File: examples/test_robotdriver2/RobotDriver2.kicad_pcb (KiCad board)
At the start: 2 copper layers, 125 x 75 mm, 68 parts, among them J1 C64658, J3 C265088, J4 C265088, J6 C64658, J7 C64658, J8 C64658, J9 C64658, SW1 C318884, U1 C7972, U2 C500769, U3 C701342, U4 C967633, U5 C50506, U6 C50506

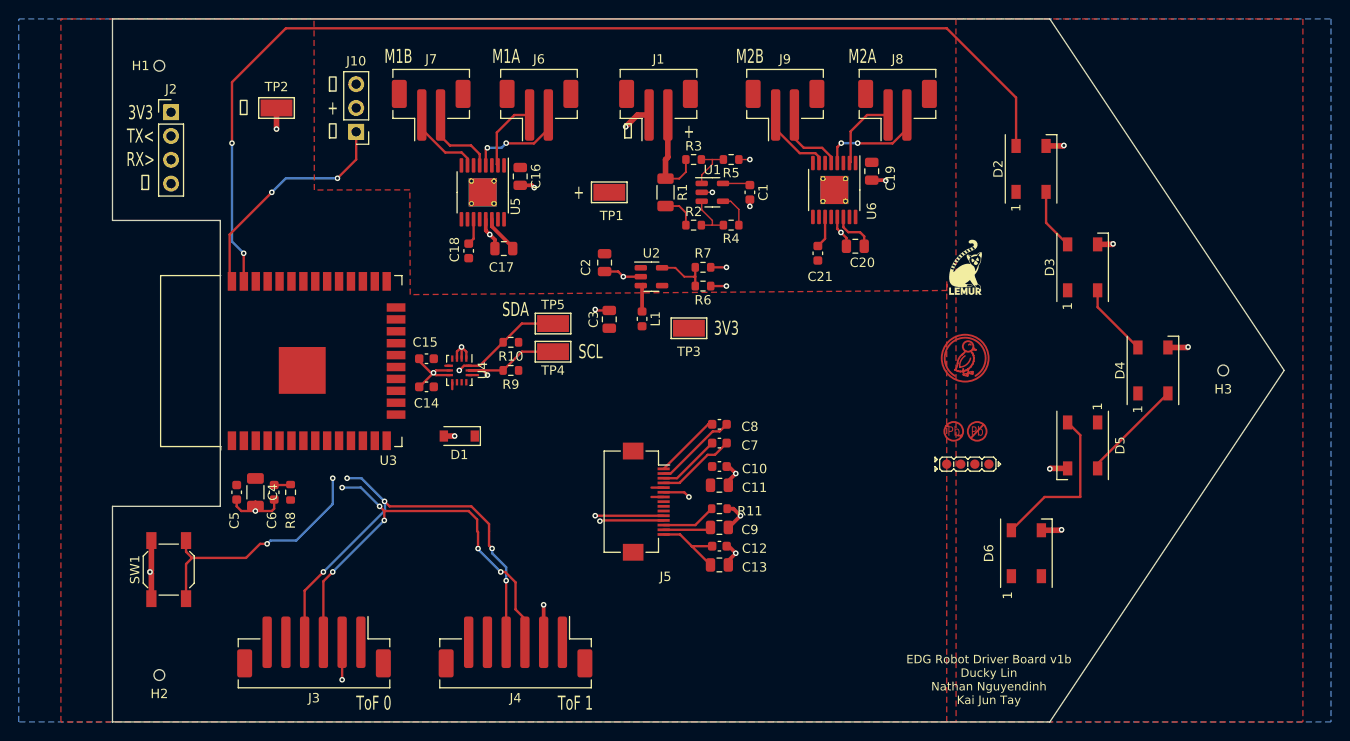
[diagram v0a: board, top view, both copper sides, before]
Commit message: robot driver 2 layout wip floorplanned
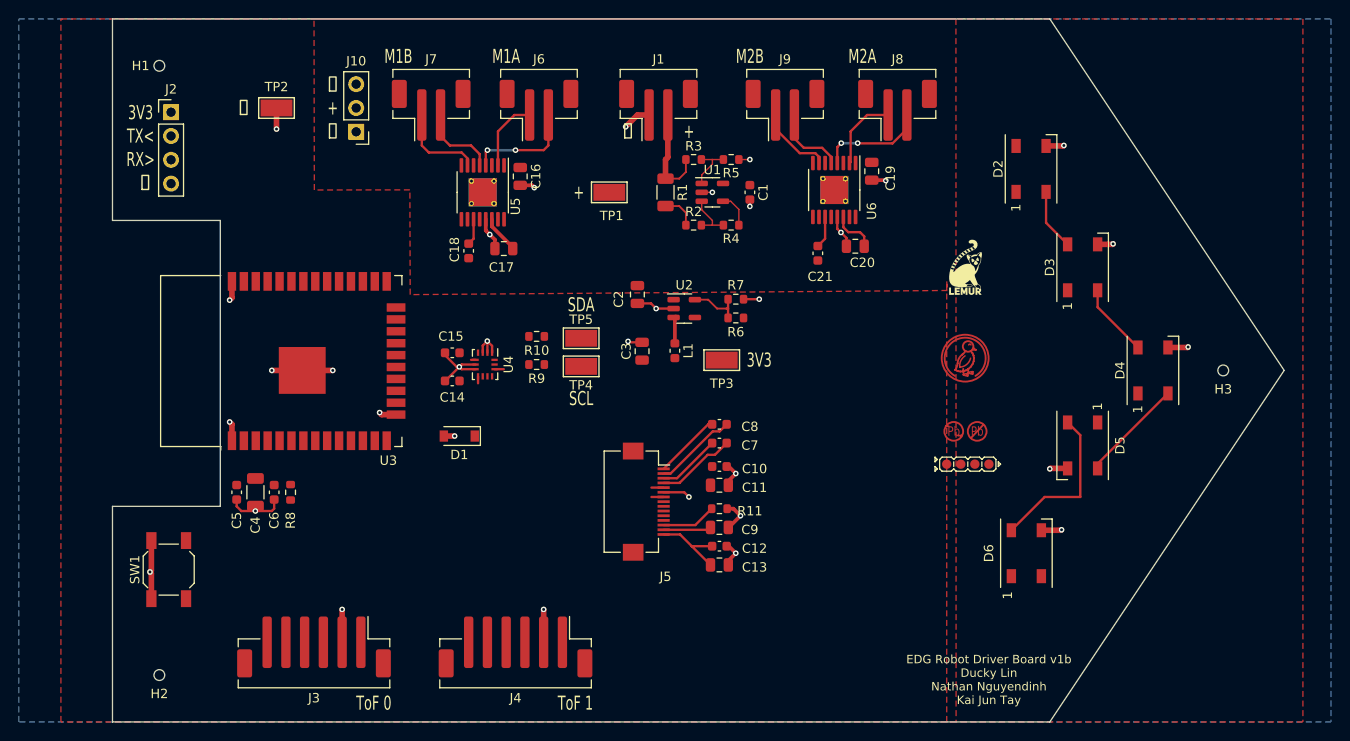
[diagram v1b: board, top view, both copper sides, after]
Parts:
- moved C2 4.88 mm to (151.0, 76.9)
- moved C3 4.88 mm to (151.5, 83.0)
- moved L1 4.88 mm to (155.0, 82.9)
- moved R6 4.88 mm to (161.5, 79.4)
- moved R7 4.88 mm to (161.5, 77.4)
- moved TP3 4.88 mm to (160.0, 83.9)
- moved U2 4.88 mm to (156.0, 78.4)
- moved TP4 3.39 mm to (145.0, 84.6)
- moved TP5 3.39 mm to (145.0, 81.6)
- moved C14 2.82 mm to (131.2, 86.1)
- moved C15 2.82 mm to (131.2, 83.1)
- moved R10 2.82 mm to (140.2, 81.4)
- moved R9 2.82 mm to (140.2, 84.4)
- moved U4 2.82 mm to (134.8, 84.4)
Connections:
- net isense.amp.(adapter)r1.b.dst renamed isense.amp.amp.inn
- net isense.amp.rg.b renamed isense.amp.amp.inp
- net lcd.c1_cap.pos renamed lcd.device.c1p
- net lcd.device.c2n renamed lcd.c2_cap.neg
- net lcd.vcc_cap1.pos renamed lcd.device.vcc
- net mcu.en_pull.output renamed mcu.ic.chip_pu
- net mcu.ic.uart0.rx renamed mcu.uart0.uart.tx
- net mcu.prog.a renamed mcu.ic.io0
- net mcu.uart0.uart.rx renamed mcu.ic.uart0.tx
- net motor_driver1.ic.vcp renamed motor_driver1.vcp_cap.pos
- net motor_driver1.ic.vint renamed motor_driver1.vint_cap.pos
- net motor_driver2.vint_cap.pwr renamed motor_driver2.vint_cap.pos
- net reg_3v3.fb.center renamed reg_3v3.ic.fb
- net reg_3v3.ic.sw renamed reg_3v3.power_path.switch
- net ws2812bArray.led[1].din renamed ws2812bArray.led[0].dout
- net ws2812bArray.led[1].dout renamed ws2812bArray.led[2].din
- U3 pad 10: mcu.gpio.motor_1a2 -> mcu.gpio.lcd_reset
- U3 pad 11: mcu.gpio.motor_2a1 -> mcu.gpio.lcd_cs
- U3 pad 12: mcu.gpio.ledArray -> i2c_chain_0.sda
- U3 pad 13: mcu.gpio.motor_2a2 -> i2c_chain_0.scl
- U3 pad 16: mcu.gpio.motor_1b1 -> mcu.adc.isense
- U3 pad 26: mcu.gpio.motor_1a1 -> mcu.gpio.motor_2a1
- U3 pad 27: mcu.gpio.motor_2b1 -> mcu.gpio.motor_2a2
- U3 pad 28: mcu.gpio.pwm -> mcu.gpio.motor_2b2
- U3 pad 29: mcu.gpio.lcd_reset -> mcu.gpio.motor_2b1
- U3 pad 30: mcu.gpio.lcd_cs -> mcu.gpio.motor_1a1
- U3 pad 31: mcu.gpio.motor_2b2 -> mcu.gpio.motor_1a2
- U3 pad 33: mcu.gpio.tof_xshut_0 -> mcu.gpio.motor_1b2
- U3 pad 36: tof.xshut.1 -> mcu.gpio.motor_1b1
- U3 pad 37: mcu.gpio.motor_1b2 -> mcu.gpio.pwm
- U3 pad 4: lcd.spi.sck -> mcu.gpio.ledArray
- U3 pad 5: lcd.spi.mosi -> mcu.gpio.tof_xshut_0
- U3 pad 6: i2c_chain_0.scl -> tof.xshut.1
- U3 pad 7: i2c_chain_0.sda -> lcd.spi.mosi
- U3 pad 8: mcu.adc.isense -> lcd.spi.sck
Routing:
- net mcu.ic.uart0.tx: track 115.8 -> 0.00 mm, vias 2 -> 0
- net i2c_chain_0.sda: track 63.3 -> 0.00 mm, vias 6 -> 0
- net i2c_chain_0.scl: track 66.0 -> 6.00 mm, vias 7 -> 0
- net mcu.ic.io0: track 26.9 -> 0.00 mm, vias 2 -> 0
- net mcu.gpio.pwm: track 24.5 -> 0.00 mm, vias 2 -> 0
- net gnd: track 81.9 -> 92.4 mm, vias 28 -> 33
- net lcd.spi.sck: track 7.30 -> 0.00 mm, vias 1 -> 0
- net lcd.spi.mosi: track 6.83 -> 0.00 mm, vias 1 -> 0
- net v3v3: track 9.93 -> 5.17 mm, vias 1 -> 0
- net mcu.ic.chip_pu: track 1.95 -> 0.00 mm
- net m1_b.pins.1: track 8.43 -> 9.46 mm
- net m1_a.pins.2: track 9.31 -> 10.2 mm

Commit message: cleanup for routing
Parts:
- renumbered 2 to U10, 1 to U9
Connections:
- net isense.amp.amp.inn renamed isense.amp.(adapter)r1.b.src
- net isense.amp.amp.inp renamed isense.amp.r2.b
- net lcd.c2_cap.pos renamed lcd.device.c2p
- net lcd.iref_res.a renamed lcd.device.iref
- net mcu.ic.chip_pu renamed mcu.en_pull.output
- net mcu.ic.io0 renamed mcu.prog.out
- net motor_driver1.vcp_cap.pos renamed motor_driver1.ic.vcp
- net motor_driver1.vint_cap.pos renamed motor_driver1.vint_cap.pwr
- net reg_3v3.ic.fb renamed reg_3v3.fb.center

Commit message: autorouted board
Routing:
- net i2c_chain_0.scl: track 6.00 -> 117.2 mm
- net mcu.gpio.ledArray: track 0.00 -> 97.1 mm
- net i2c_chain_0.sda: track 0.00 -> 83.6 mm, vias 0 -> 2
- net v3v3: track 5.17 -> 75.7 mm, vias 0 -> 10
- net mcu.gpio.motor_2a2: track 0.00 -> 62.7 mm
- net mcu.gpio.motor_2a1: track 0.00 -> 56.5 mm, vias 0 -> 2
- net mcu.gpio.motor_2b1: track 0.00 -> 55.5 mm
- net mcu.gpio.motor_2b2: track 0.00 -> 55.0 mm
- net mcu.prog.out: track 0.00 -> 49.3 mm
- net mcu.adc.isense: track 3.72 -> 50.8 mm, vias 0 -> 2
- net lcd.spi.mosi: track 0.00 -> 42.7 mm
- net lcd.spi.sck: track 0.00 -> 41.2 mm
- net mcu.gpio.lcd_dc: track 0.00 -> 39.7 mm
- net batt.pins.2: track 10.7 -> 50.0 mm
- net mcu.gpio.lcd_reset: track 0.00 -> 38.3 mm
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
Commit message: robot driver 2
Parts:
- R4, R5: value C25804 -> C25803
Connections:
- net isense.amp.(adapter)r1.b.src renamed isense.amp.(adapter)rf.b.dst
- net isense.amp.r2.b renamed isense.amp.rg.b
- net lcd.c1_cap.neg renamed lcd.device.c1n
- net lcd.device.vcc renamed lcd.vcc_cap2.pos
- net mcu.ic.uart0.tx renamed mcu.uart0.uart.rx
- net motor_driver2.vint_cap.pos renamed motor_driver2.vint_cap.pwr
- net tof.xshut.1 renamed mcu.gpio.tof_xshut_1
- net ws2812bArray.led[0].dout renamed ws2812bArray.led[1].din
- net ws2812bArray.led[2].din renamed ws2812bArray.led[1].dout
- net ws2812bArray.led[2].dout renamed ws2812bArray.led[3].din
